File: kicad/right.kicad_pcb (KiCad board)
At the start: 4 copper layers, 137.5 x 109.3 mm, 123 parts, among them Q1 PMF170XP,115, Q2 FS8205A_C2830320, SW1 TS-1088-AR02016, U1 E73-2G4M08S1C, U10 DW01A_C42380662, U2 LP5024RSMR, U3 IP2312, U4 SN74LVC1G74DQER, U5 SN74LVC1G17DBVR, U6 SMF5.0A, U7 USBLC6-2SC6, U8 S2B-PH-K-S(LF)(SN), U9 MAX17048, X1 FC-13532.768KHZ9PF20PPM

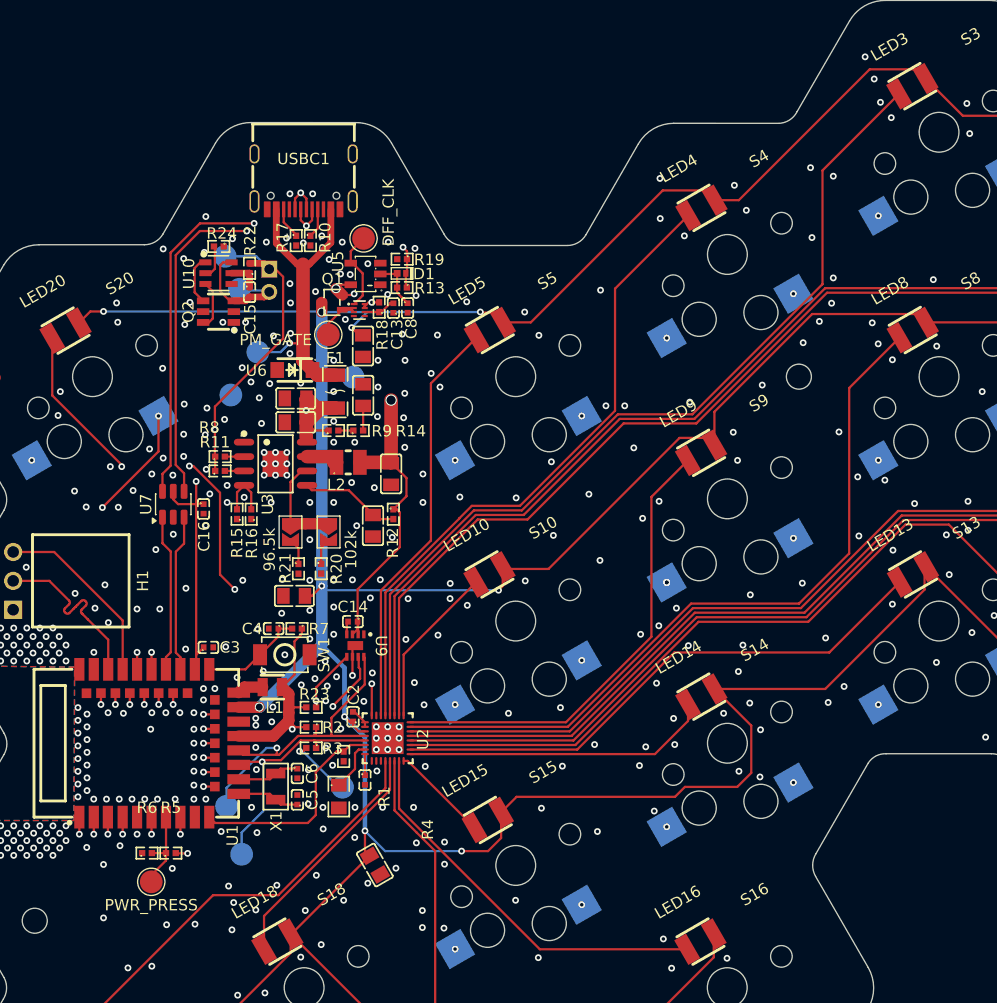
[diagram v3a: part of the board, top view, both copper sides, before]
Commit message: ran DRC abd fixed accordingely
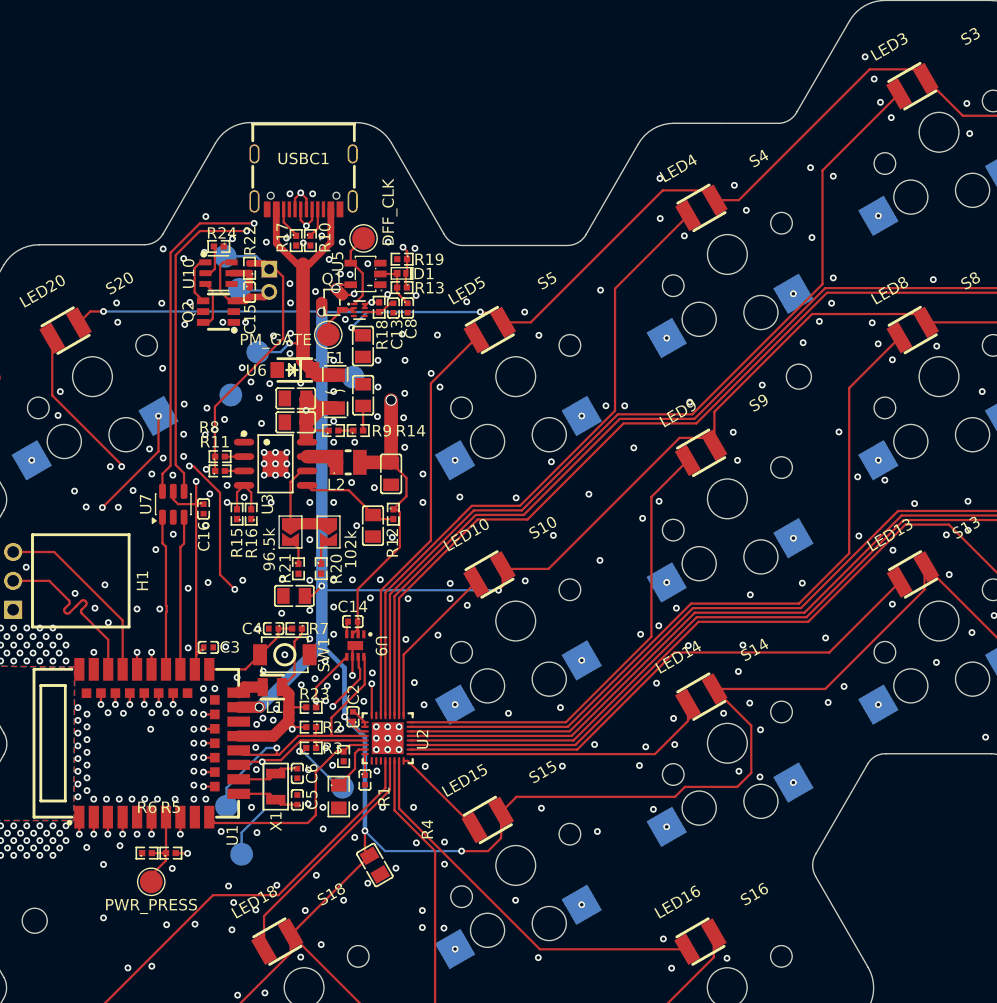
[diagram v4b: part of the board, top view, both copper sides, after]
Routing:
- net /PWR: track 528.8 -> 522.7 mm
- net /BAT+: track 105.1 -> 102.9 mm
- net GND: track 7.14 -> 5.08 mm, vias 517 -> 519
- net /BAT-: track 12.6 -> 11.0 mm
- net /VBUS: track 49.1 -> 47.8 mm
- net /ICHG: track 9.38 -> 8.40 mm
- net /PWR_BTN_PRESS: track 7.47 -> 6.89 mm
- net Net-(U3-BAT): track 8.82 -> 8.24 mm
- net /LED20: track 50.5 -> 51.0 mm
- net /S9: vias 4 -> 2
